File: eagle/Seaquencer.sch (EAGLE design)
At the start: 48 parts, among them IC1 ATMEGA48/88/168, IC2 74HC595N

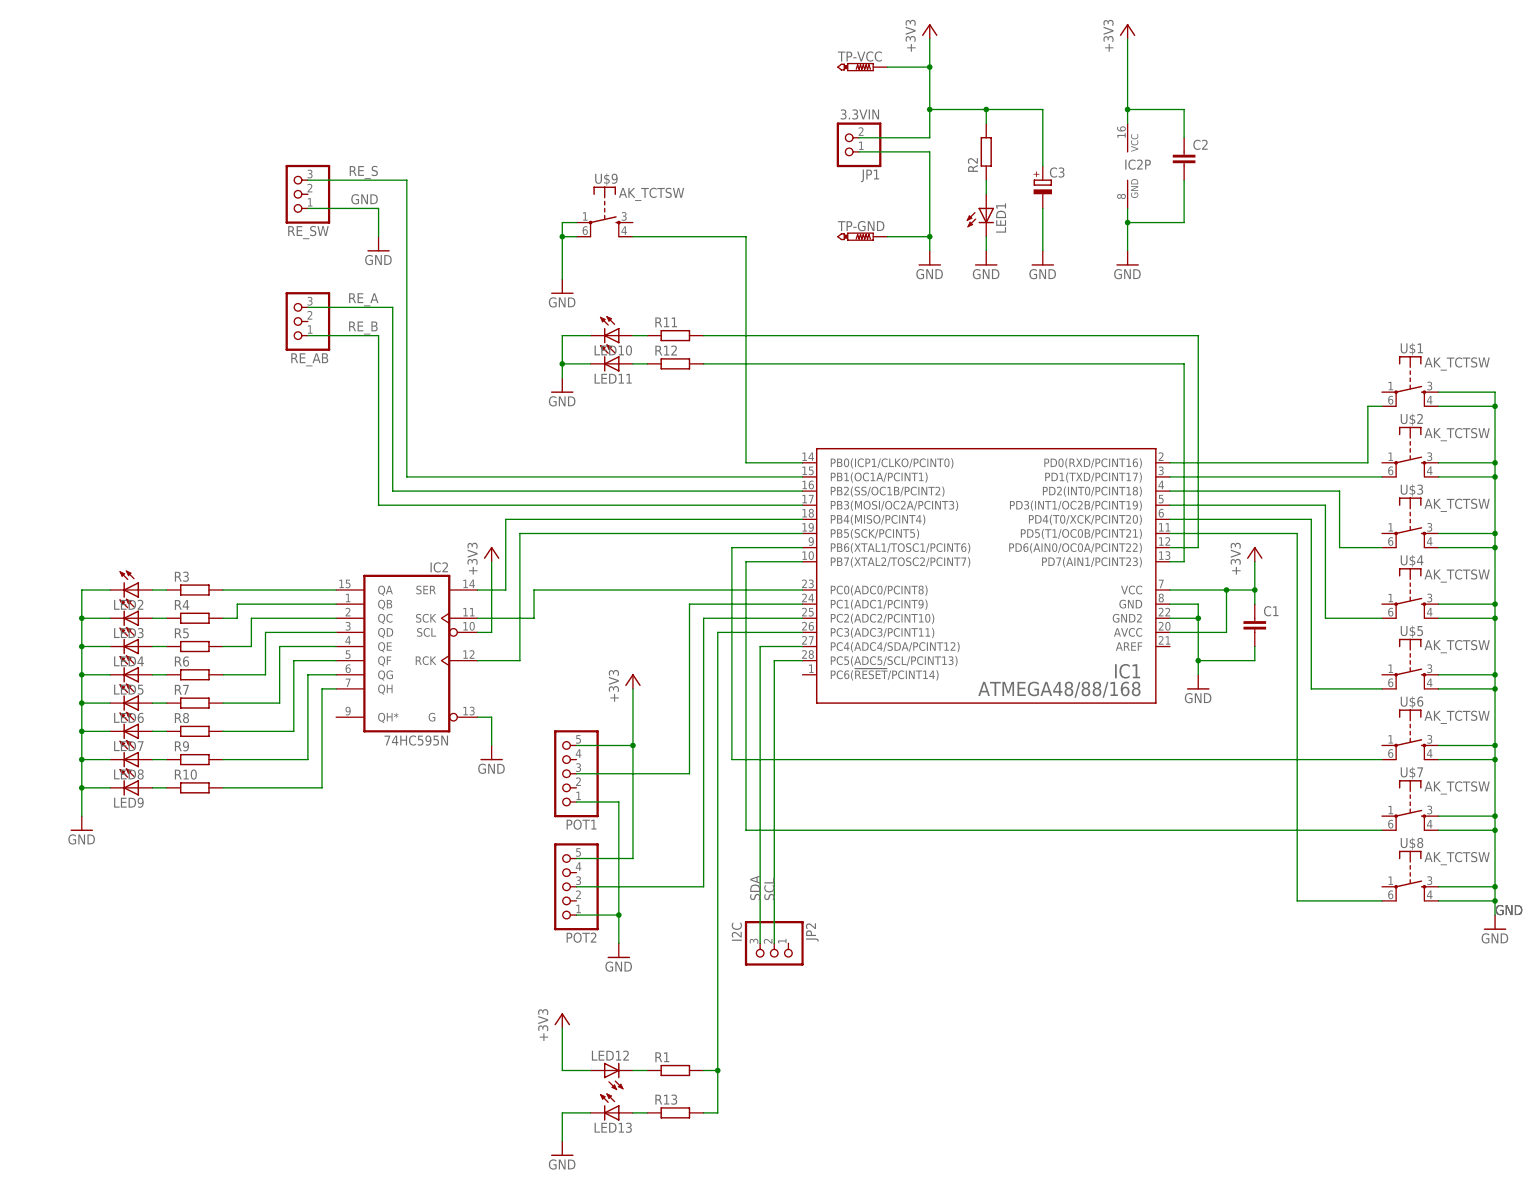
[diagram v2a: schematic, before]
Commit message: 回路図、基板図： Valueを設定
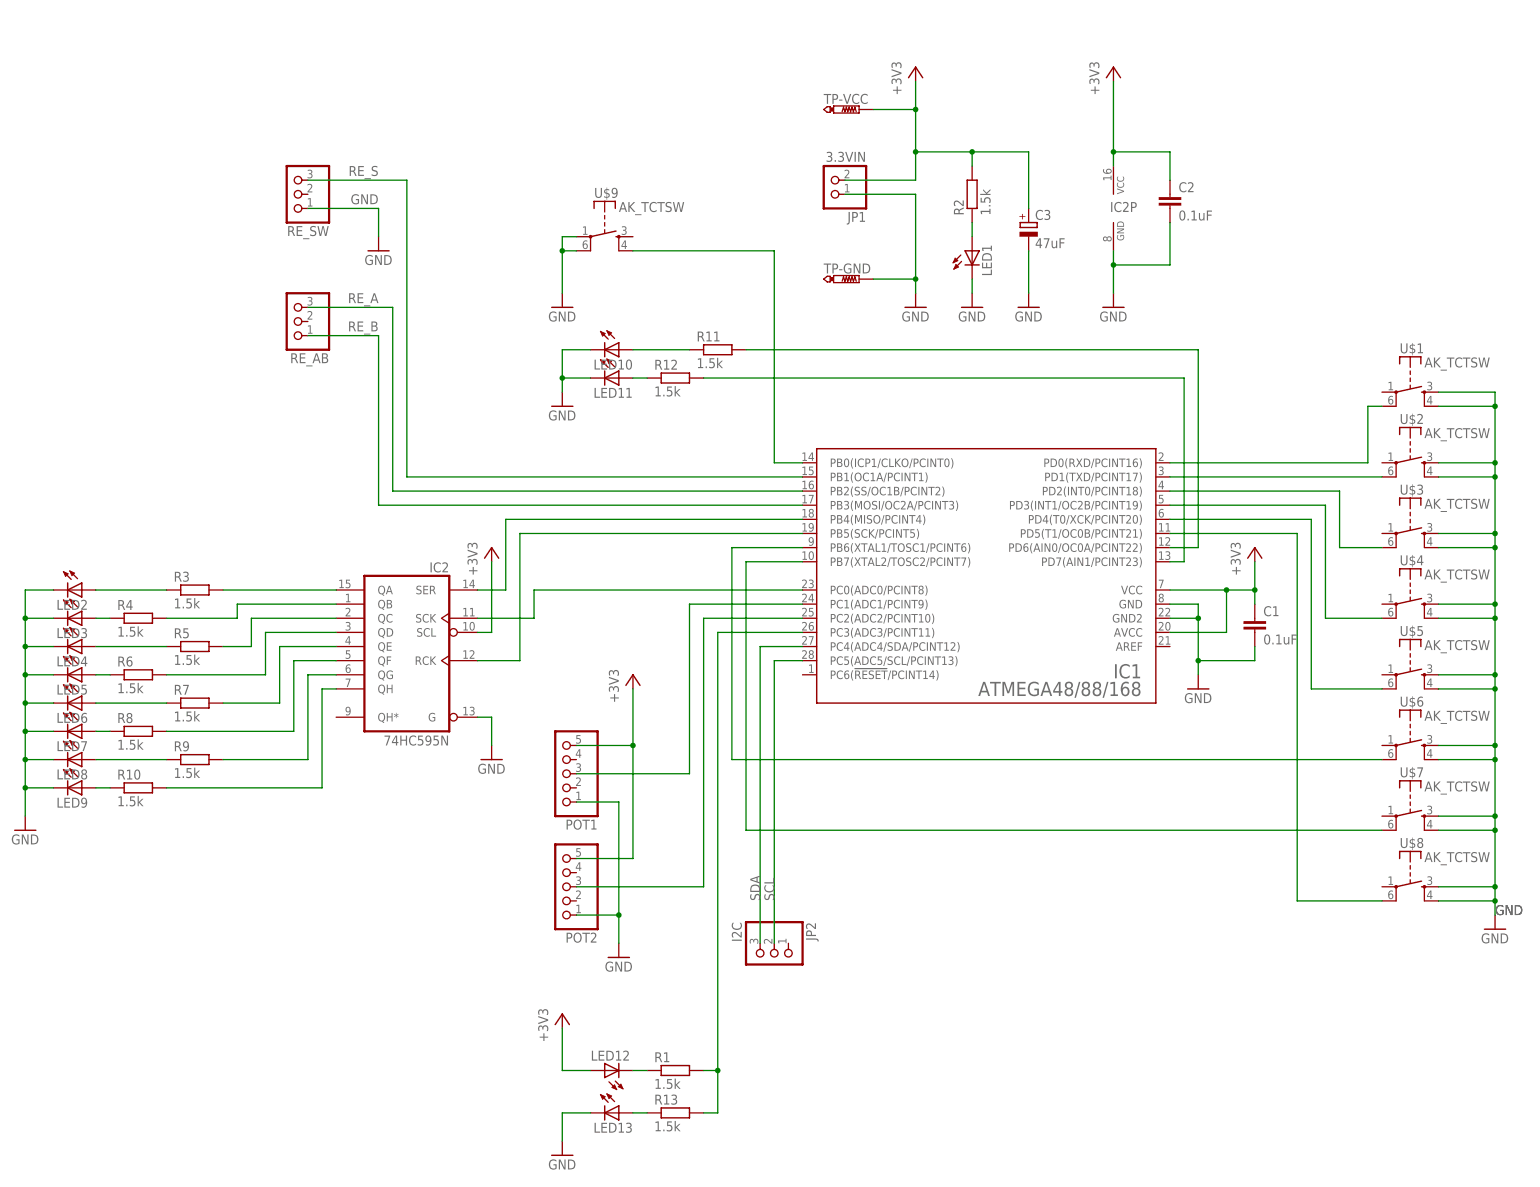
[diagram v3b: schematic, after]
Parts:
- C1, C2: value (none) -> 0.1uF
- C3: value (none) -> 47uF
- R1, R10, R11, R12, R13, R2, R3, R4, R5, R6, R7, R8, R9: value (none) -> 1.5k
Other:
- moved on the sheet: C2, C3, IC2P, JP1, LED1, LED10, LED11, LED2, LED3, LED4, LED5, LED6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

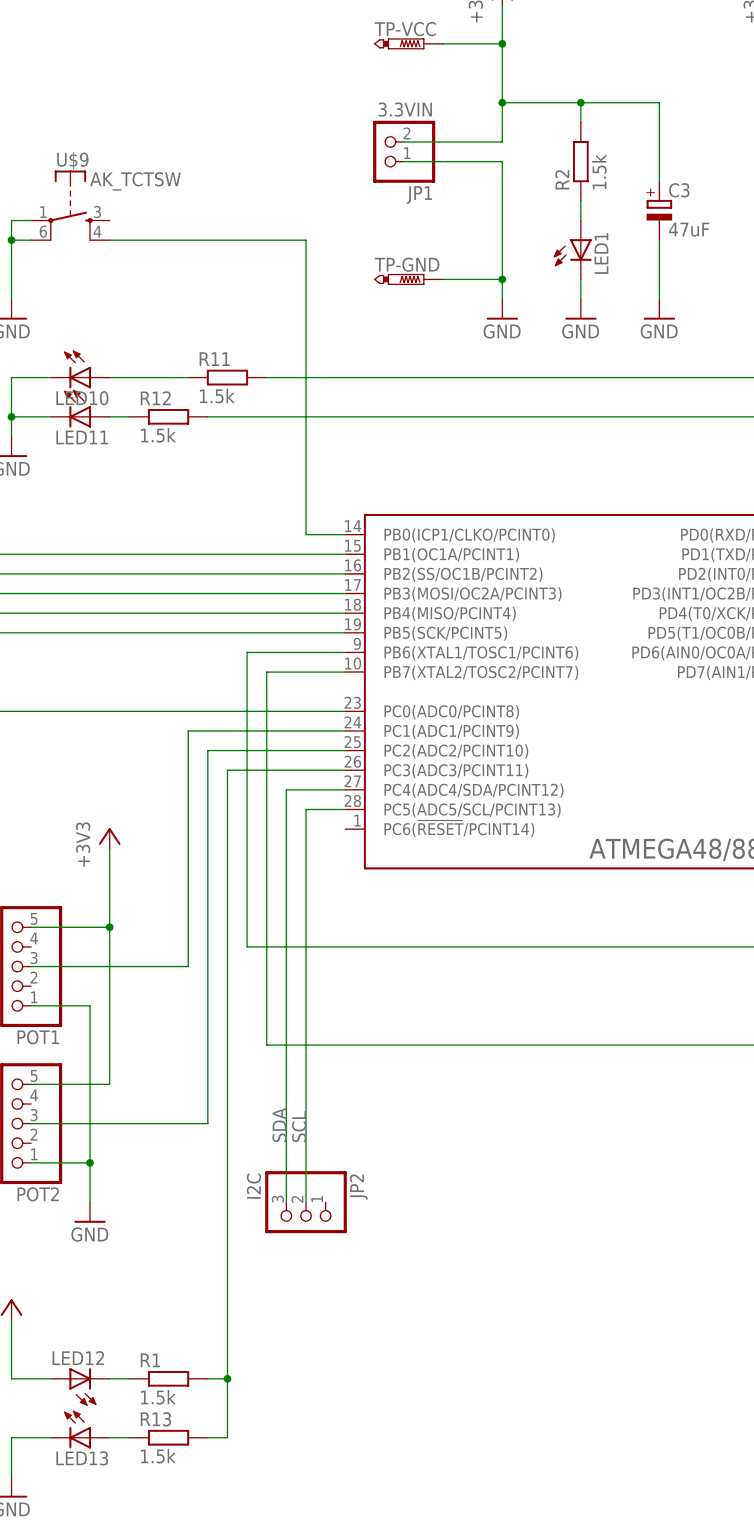
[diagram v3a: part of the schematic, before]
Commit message: 抵抗値変更
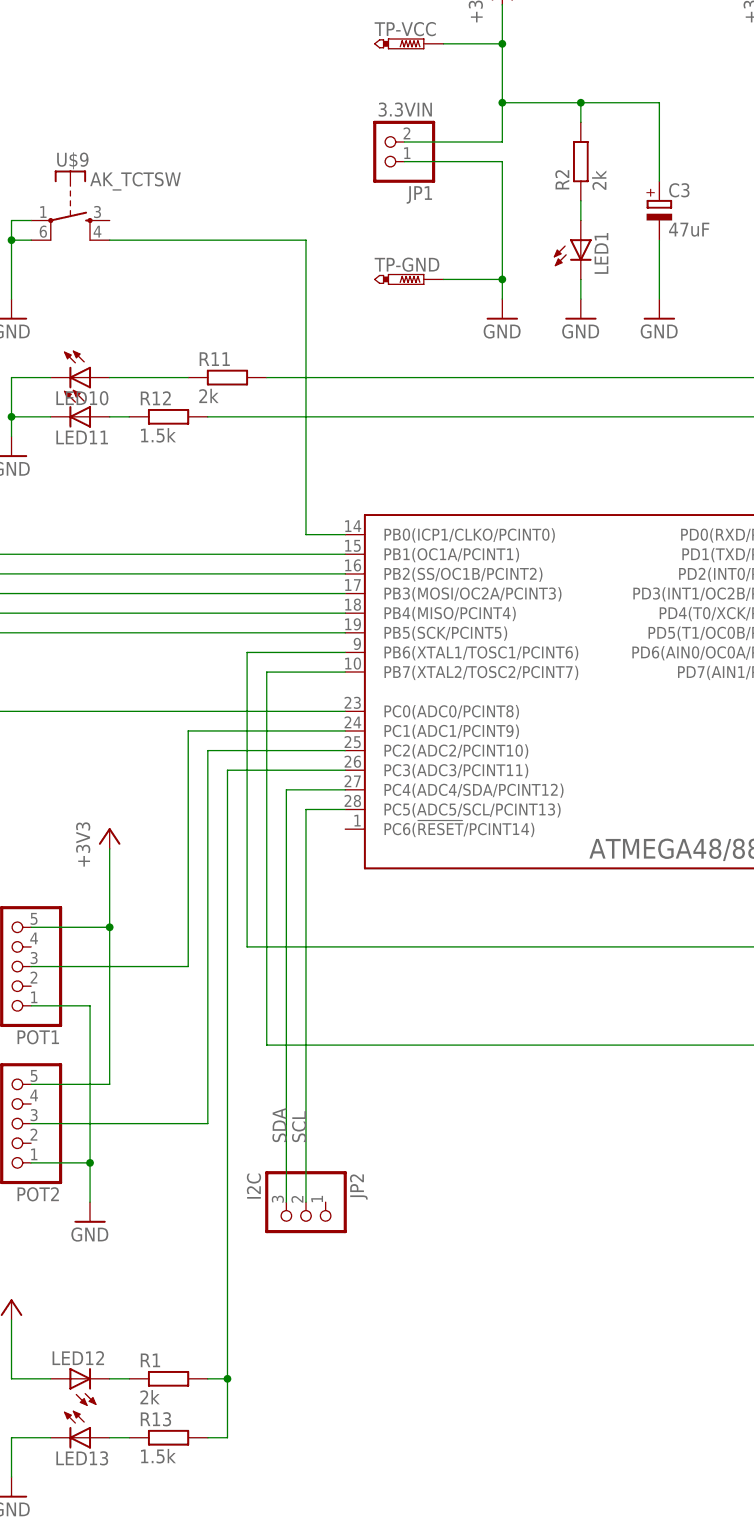
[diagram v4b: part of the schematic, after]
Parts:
- R1, R11, R2: value 1.5k -> 2k
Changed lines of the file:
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@@
 <part name="IC2" library="74xx-eu" deviceset="74*595" device="N" technology="HC"/>
 <part name="+3V3" library="supply1" deviceset="+3V3" device=""/>
-<part name="R2" library="rcl" deviceset="R-EU_" device="0207/7" value="1.5k"/>
+<part name="R2" library="rcl" deviceset="R-EU_" device="0207/7" value="2k"/>
 <part name="LED1" library="led" deviceset="LED" device="3MM"/>
 <part name="GND4" library="supply1" deviceset="GND" device=""/>
@@
 <part name="LED9" library="led" deviceset="LED" device="3MM"/>
 <part name="GND5" library="supply1" deviceset="GND" device=""/>
-<part name="R11" library="rcl" deviceset="R-EU_" device="0207/7" value="1.5k"/>
+<part name="R11" library="rcl" deviceset="R-EU_" device="0207/7" value="2k"/>
 <part name="R12" library="rcl" deviceset="R-EU_" device="0207/7" value="1.5k"/>
 <part name="LED10" library="led" deviceset="LED" device="3MM"/>
@@
 <part name="POT2" library="pinhead" deviceset="PINHD-1X5" device=""/>
 <part name="LED12" library="led" deviceset="LED" device="3MM"/>
-<part name="R1" library="rcl" deviceset="R-EU_" device="0207/7" value="1.5k"/>
+<part name="R1" library="rcl" deviceset="R-EU_" device="0207/7" value="2k"/>
 <part name="LED13" library="led" deviceset="LED" device="3MM"/>
 <part name="R13" library="rcl" deviceset="R-EU_" device="0207/7" value="1.5k"/>

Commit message: Sequencer.brd: Rotary Encoder付近のLEDの位置を変更
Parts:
- JP1: device pinhead:PINHD-1X2 -> pinhead:PINHD-1X2/90
- JP2: device pinhead:PINHD-1X3 -> pinhead:PINHD-1X3/90
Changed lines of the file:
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@@
 <setting verticaltext="up"/>
 </settings>
-<grid distance="0.1" unitdist="inch" unit="inch" style="dots" multiple="1" display="yes" altdistance="0.01" altunitdist="inch" altunit="inch"/>
+<grid distance="0.1" unitdist="inch" unit="inch" style="lines" multiple="1" display="no" altdistance="0.01" altunitdist="inch" altunit="inch"/>
 <layers>
 <layer number="1" name="Top" color="4" fill="1" visible="no" active="no"/>
@@
 <part name="U$7" library="mylib" deviceset="AK_TCTSW" device=""/>
 <part name="U$8" library="mylib" deviceset="AK_TCTSW" device=""/>
-<part name="JP1" library="pinhead" deviceset="PINHD-1X2" device="" value="3.3VIN"/>
+<part name="JP1" library="pinhead" deviceset="PINHD-1X2" device="/90" value="3.3VIN"/>
 <part name="+3V1" library="supply1" deviceset="+3V3" device=""/>
 <part name="GND1" library="supply1" deviceset="GND" device=""/>
@@
 <part name="RE_AB" library="pinhead" deviceset="PINHD-1X3" device=""/>
 <part name="RE_SW" library="pinhead" deviceset="PINHD-1X3" device=""/>
-<part name="JP2" library="pinhead" deviceset="PINHD-1X3" device="" value="I2C"/>
+<part name="JP2" library="pinhead" deviceset="PINHD-1X3" device="/90" value="I2C"/>
 <part name="+3V5" library="supply1" deviceset="+3V3" device=""/>
 <part name="GND11" library="supply1" deviceset="GND" device=""/>
